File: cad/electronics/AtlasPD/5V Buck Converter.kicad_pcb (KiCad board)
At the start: 2 copper layers, 93.5 x 50.4 mm, 33 parts, among them J401 Conn_01x04, Q401 Q_Dual_NMOS_S1G1S2G2D2D2D1D1, U401 AP1509-50SG-13, U402 DS2777

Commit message: Refined PCB design, want to do final review later on before sending to Fab
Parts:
- added REF**: ESD-Logo_6.6x6mm_SilkScreen, Symbol:ESD-Logo_6.6x6mm_SilkScreen, F.Cu at (28.0, 73.4)
- added REF**: WEEE-Logo_4.2x6mm_SilkScreen, Symbol:WEEE-Logo_4.2x6mm_SilkScreen, F.Cu at (37.6, 73.3)
- added REF**: KiCad-Logo_5mm_Copper, Symbol:KiCad-Logo_5mm_Copper, B.Cu at (92.9, 79.1)
- R406: value RSNS -> 20m; footprint Resistor_SMD:R_0805_2012Metric -> Resistor_THT:R_Box_L13.0mm_W4.0mm_P9.00mm
- moved R406 2.49 mm to (71.8, 76.1), turned to 90 degrees
- moved U402 2.14 mm to (74.2, 80.3)
- moved REF** 1.88 mm to (19.8, 73.8)
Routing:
- net GND: track 2.34 -> 8.26 mm, vias 123 -> 121
- net Net-(C404-Pad1): track 17.1 -> 20.4 mm
- net /SRC: track 32.0 -> 34.6 mm
- net Net-(R407-Pad2): track 12.2 -> 14.5 mm
- net Net-(C403-Pad1): track 10.0 -> 7.95 mm
- net Net-(R401-Pad2): track 8.40 -> 10.0 mm
- net Net-(C405-Pad1): track 9.45 -> 10.8 mm
- net Net-(D402-Pad1): track 24.8 -> 25.9 mm
- net GNDPWR: track 10.1 -> 9.21 mm, vias 14 -> 13
- net Net-(D403-Pad2): track 10.8 -> 11.7 mm
- net Net-(R402-Pad2): track 10.7 -> 11.3 mm

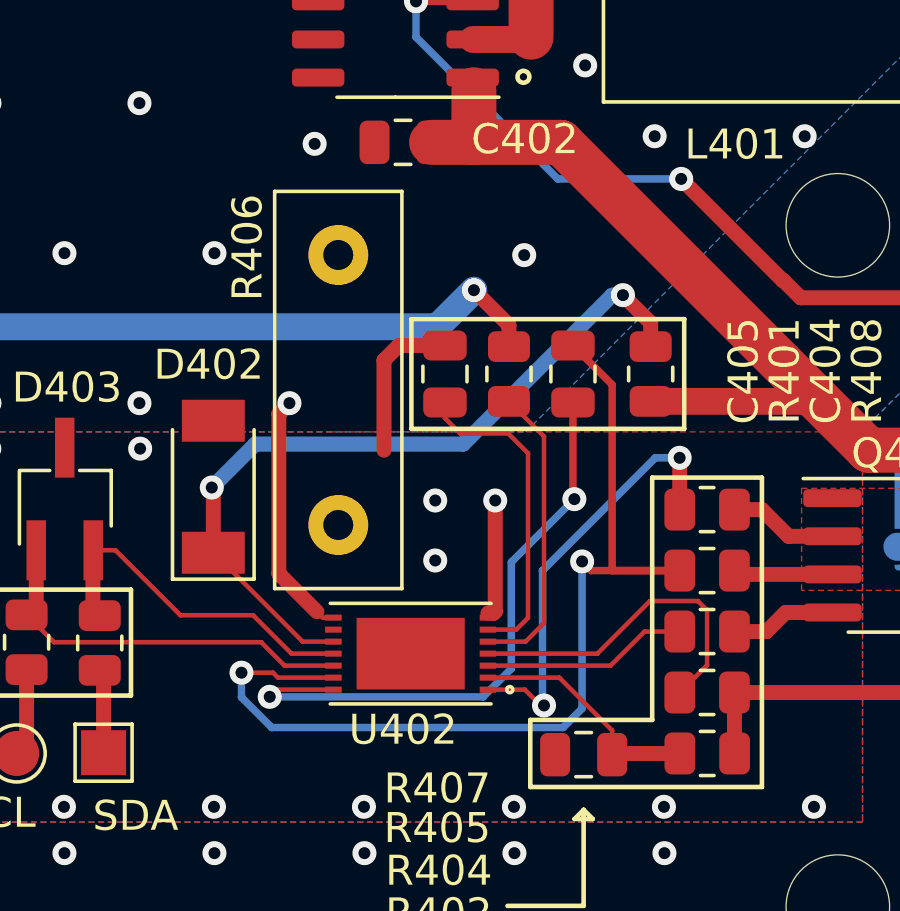
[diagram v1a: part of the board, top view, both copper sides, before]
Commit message: Simplified design layout
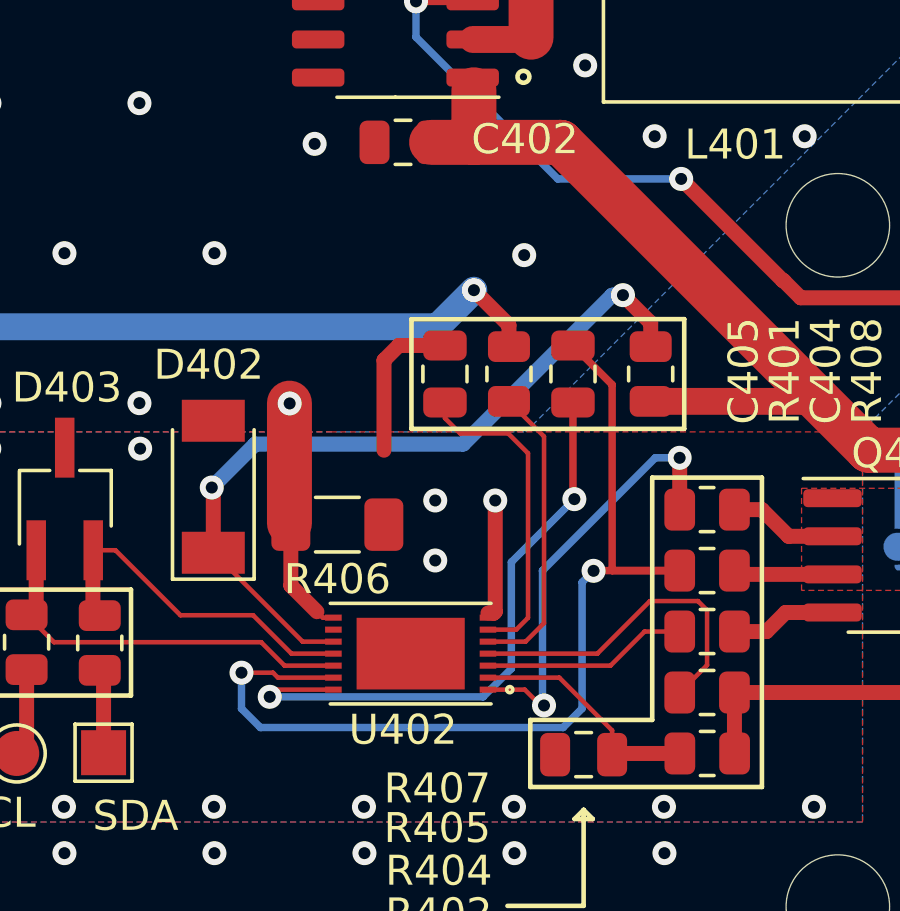
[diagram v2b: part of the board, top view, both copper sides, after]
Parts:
- R406: footprint Resistor_THT:R_Box_L13.0mm_W4.0mm_P9.00mm -> Resistor_SMD:R_1206_3216Metric_Pad1.30x1.75mm_HandSolder
- turned R406 to 180 degrees
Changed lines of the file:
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@@
       (net 23 "/SDA") (pinfunction "1") (pintype "passive"))
   )
+  (footprint "Resistor_SMD:R_1206_3216Metric_Pad1.30x1.75mm_HandSolder" (layer "F.Cu")
+    (at 71.75 76.04 180)
+    (descr "Resistor SMD 1206 (3216 Metric), square (rectangular) end terminal, IPC_7351 nominal with elongated pad for handsoldering. (Body size source: IPC-SM-782 page 72, https://www.pcb-3d.com/wordpress/wp-content/uploads/ipc-sm-782a_amendment_1_and_2.pdf), generated with kicad-footprint-generator")
+    (tags "resistor handsolder")
+    (property "Sheetfile" "5V Buck Converter.kicad_sch")
+    (property "Sheetname" "")
+    (attr smd)
+    (fp_text reference "R406" (at 0 -1.82) (layer "F.SilkS")
+      (effects (font (size 1 1) (thickness 0.15)))
+    )
+    (fp_text value "20m" (at 0 1.82) (layer "F.Fab")
+      (effects (font (size 1 1) (thickness 0.15)))
+    )
+    (fp_text user "${REFERENCE}" (at 0 0) (layer "F.Fab")
+      (effects (font (size 0.8 0.8) (thickness 0.12)))
+    )
+    (fp_line (start -0.727064 -0.91) (end 0.727064 -0.91) (layer "F.SilkS") (width 0.12))
+    (fp_line (start -0.727064 0.91) (end 0.727064 0.91) (layer "F.SilkS") (width 0.12))
+    (fp_line (start -2.45 -1.12) (end 2.45 -1.12) (layer "F.CrtYd") (width 0.05))
+    (fp_line (start -2.45 1.12) (end -2.45 -1.12) (layer "F.CrtYd") (width 0.05))
+    (fp_line (start 2.45 -1.12) (end 2.45 1.12) (layer "F.CrtYd") (width 0.05))
+    (fp_line (start 2.45 1.12) (end -2.45 1.12) (layer "F.CrtYd") (width 0.05))
+    (fp_line (start 1.6 -0.8) (end 1.6 0.8) (layer "F.Fab") (width 0.1))
+    (fp_line (start -1.6 -0.8) (end 1.6 -0.8) (layer "F.Fab") (width 0.1))
+    (fp_line (start 1.6 0.8) (end -1.6 0.8) (layer "F.Fab") (width 0.1))
+    (fp_line (start -1.6 0.8) (end -1.6 -0.8) (layer "F.Fab") (width 0.1))
+    (pad "1" smd roundrect locked (at -1.55 0 180) (size 1.3 1.75) (layers "F.Cu" "F.Paste" "F.Mask") (roundrect_rratio 0.192308)
+      (net 8 "GNDPWR") (pintype "passive"))
+    (pad "2" smd roundrect locked (at 1.55 0 180) (size 1.3 1.75) (layers "F.Cu" "F.Paste" "F.Mask") (roundrect_rratio 0.192308)
+      (net 1 "GND") (pintype "passive"))
+    (model "${KICAD6_3DMODEL_DIR}/Resistor_SMD.3dshapes/R_1206_3216Metric.wrl"
+      (offset (xyz 0 0 0))
+      (scale (xyz 1 1 1))
+      (rotate (xyz 0 0 0))
+    )
+  )
   (footprint "Package_TO_SOT_SMD:TSOT-23_HandSoldering" (layer "F.Cu")
     (at 62.6618 75.184 90)
@@
     )
   )
-  (footprint "Resistor_THT:R_Box_L13.0mm_W4.0mm_P9.00mm" (layer "F.Cu")
-    (at 71.7804 76.0518 90)
-    (descr "Resistor, Box series, Radial, pin pitch=9.00mm, 2W, length*width=13.0*4.0mm^2, http://www.produktinfo.conrad.com/datenblaetter/425000-449999/443860-da-01-de-METALLBAND_WIDERSTAND_0_1_OHM_5W_5Pr.pdf")
-    (tags "Resistor Box series Radial pin pitch 9.00mm 2W length 13.0mm width 4.0mm")
-    (property "Sheetfile" "5V Buck Converter.kicad_sch")
-    (property "Sheetname" "")
-    (attr through_hole)
-    (fp_text reference "R406" (at 9.2498 -3.0226 90) (layer "F.SilkS")
-      (effects (font (size 1 1) (thickness 0.15)))
-    )
-    (fp_text value "20m" (at 4.5 3.25 90) (layer "F.Fab")
-      (effects (font (size 1 1) (thickness 0.15)))
-    )
-    (fp_text user "${REFERENCE}" (at 4.5 0 90) (layer "F.Fab")
-      (effects (font (size 1 1) (thickness 0.15)))
-    )
-    (fp_line (start 11.12 -2.12) (end 11.12 2.12) (layer "F.SilkS") (width 0.12))
-    (fp_line (start -2.12 -2.12) (end 11.12 -2.12) (layer "F.SilkS") (width 0.12))
-    (fp_line (start -2.12 2.12) (end 11.12 2.12) (layer "F.SilkS") (width 0.12))
-    (fp_line (start -2.12 -2.12) (end -2.12 2.12) (layer "F.SilkS") (width 0.12))
-    (fp_line (start 11.25 -2.25) (end -2.25 -2.25) (layer "F.CrtYd") (width 0.05))
-    (fp_line (start -2.25 -2.25) (end -2.25 2.25) (layer "F.CrtYd") (width 0.05))
-    (fp_line (start -2.25 2.25) (end 11.25 2.25) (layer "F.CrtYd") (width 0.05))
-    (fp_line (start 11.25 2.25) (end 11.25 -2.25) (layer "F.CrtYd") (width 0.05))
-    (fp_line (start -2 2) (end 11 2) (layer "F.Fab") (width 0.1))
-    (fp_line (start 11 2) (end 11 -2) (layer "F.Fab") (width 0.1))
-    (fp_line (start -2 -2) (end -2 2) (layer "F.Fab") (width 0.1))
-    (fp_line (start 11 -2) (end -2 -2) (layer "F.Fab") (width 0.1))
-    (pad "1" thru_hole circle locked (at 0 0 90) (size 2 2) (drill 1) (layers *.Cu *.Mask)
-      (net 8 "GNDPWR") (pintype "passive"))
-    (pad "2" thru_hole circle locked (at 9 0 90) (size 2 2) (drill 1) (layers *.Cu *.Mask)
-      (net 1 "GND") (pintype "passive"))
-    (model "${KICAD6_3DMODEL_DIR}/Resistor_THT.3dshapes/R_Box_L13.0mm_W4.0mm_P9.00mm.wrl"
-      (offset (xyz 0 0 0))
-      (scale (xyz 1 1 1))
-      (rotate (xyz 0 0 0))
-    )
-  )
   (footprint "Resistor_SMD:R_0805_2012Metric" (layer "F.Cu")
     (at 84.079 83.6676 180)
@@
     (style (thickness 0.15) (arrow_length 1.27) (text_position_mode 0) (extension_height 0.58642) (extension_offset 0) keep_text_aligned)
   )
+  (segment (start 71.0692 78.9432) (end 70.2 78.074) (width 0.5) (layer "F.Cu") (net 1))
   (segment (start 71.2662 79.1402) (end 71.6177 79.1402) (width 0.1524) (layer "F.Cu") (net 1))
-  (segment (start 71.0692 78.9432) (end 69.7992 77.6732) (width 0.5) (layer "F.Cu") (net 1))
+  (segment (start 70.2 78.074) (end 70.2 76.04) (width 0.5) (layer "F.Cu") (net 1))
+  (segment (start 70.153 71.99) (end 70.153 75.993) (width 1.5) (layer "F.Cu") (net 1))
   (segment (start 71.0692 78.9432) (end 71.2662 79.1402) (width 0.1524) (layer "F.Cu") (net 1))
-  (segment (start 69.7992 77.6732) (end 69.7992 72.3438) (width 0.5) (layer "F.Cu") (net 1))
-  (segment (start 69.7992 72.3438) (end 70.153 71.99) (width 0.5) (layer "F.Cu") (net 1))
+  (segment (start 70.153 75.993) (end 70.2 76.04) (width 0.5) (layer "F.Cu") (net 1))
   (via (at 22.653 46.99) (size 0.8) (drill 0.4) (layers "F.Cu" "B.Cu") (net 1))
   (via (at 27.653 46.99) (size 0.8) (drill 0.4) (layers "F.Cu" "B.Cu") (net 1))
@@
   (via (at 67.653 66.99) (size 0.8) (drill 0.4) (layers "F.Cu" "B.Cu") (net 1))
   (via (at 77.978 67.056) (size 0.8) (drill 0.4) (layers "F.Cu" "B.Cu") (net 1))
-  (via (at 70.153 71.99) (size 0.8) (drill 0.4) (layers "F.Cu" "B.Cu") (net 1))
+  (via (at 70.16 72) (size 0.8) (drill 0.4) (layers "F.Cu" "B.Cu") (net 1))
   (via (at 65.153 71.99) (size 0.8) (drill 0.4) (layers "F.Cu" "B.Cu") (net 1))
   (via (at 80.01 60.7314) (size 0.8) (drill 0.4) (layers "F.Cu" "B.Cu") (net 1))
@@
   (segment (start 77.55 80.84) (end 76.610556 81.779444) (width 0.25) (layer "B.Cu") (net 10))
   (segment (start 77.55 77.29) (end 77.55 80.84) (width 0.25) (layer "B.Cu") (net 10))
-  (segment (start 80.2132 77.5716) (end 83.1615 77.5716) (width 0.25) (layer "F.Cu") (net 11))
+  (segment (start 80.29 77.58) (end 80.2984 77.5716) (width 0.25) (layer "F.Cu") (net 11))
   (segment (start 80.909089 77.5716) (end 83.1615 77.5716) (width 0.25) (layer "F.Cu") (net 11))
   (segment (start 71.6177 81.140201) (end 69.770201 81.140201) (width 0.1524) (layer "F.Cu") (net 11))
+  (segment (start 80.2984 77.5716) (end 83.1615 77.5716) (width 0.25) (layer "F.Cu") (net 11))
   (segment (start 69.6052 80.9752) (end 68.5546 80.9752) (width 0.1524) (layer "F.Cu") (net 11))
   (segment (start 80.909089 71.373889) (end 80.909089 77.5716) (width 0.25) (layer "F.Cu") (net 11))
   (segment (start 69.770201 81.140201) (end 69.6052 80.9752) (width 0.1524) (layer "F.Cu") (net 11))
   (segment (start 79.6036 70.0684) (end 80.909089 71.373889) (width 0.25) (layer "F.Cu") (net 11))
-  (segment (start 79.9084 77.2668) (end 80.2132 77.5716) (width 0.25) (layer "F.Cu") (net 11))
-  (via (at 79.9084 77.2668) (size 0.8) (drill 0.4) (layers "F.Cu" "B.Cu") (net 11))
+  (via (at 80.29 77.58) (size 0.8) (drill 0.4) (layers "F.Cu" "B.Cu") (net 11))
   (via (at 68.5546 80.9752) (size 0.8) (drill 0.4) (layers "F.Cu" "B.Cu") (net 11))
-  (segment (start 79.9084 82.169) (end 79.9084 77.2668) (width 0.25) (layer "B.Cu") (net 11))
-  (segment (start 69.564249 82.804) (end 79.2734 82.804) (width 0.25) (layer "B.Cu") (net 11))
-  (segment (start 68.5546 81.794351) (end 69.564249 82.804) (width 0.25) (layer "B.Cu") (net 11))
-  (segment (start 79.2734 82.804) (end 79.9084 82.169) (width 0.25) (layer "B.Cu") (net 11))
-  (segment (start 68.5546 80.9752) (end 68.5546 81.794351) (width 0.25) (layer "B.Cu") (net 11))
+  (segment (start 80.29 77.58) (end 79.9084 77.9616) (width 0.25) (layer "B.Cu") (net 11))
+  (segment (start 79.2734 82.804) (end 69.184 82.804) (width 0.25) (layer "B.Cu") (net 11))
+  (segment (start 79.9084 82.169) (end 79.2734 82.804) (width 0.25) (layer "B.Cu") (net 11))
+  (segment (start 69.184 82.804) (end 68.5546 82.1746) (width 0.25) (layer "B.Cu") (net 11))
+  (segment (start 68.5546 82.1746) (end 68.5546 80.9752) (width 0.25) (layer "B.Cu") (net 11))
+  (segment (start 79.9084 77.9616) (end 79.9084 82.169) (width 0.25) (layer "B.Cu") (net 11))
   (segment (start 75.3364 72.4916) (end 75.8444 72.9996) (width 0.1524) (layer "F.Cu") (net 12))
   (segment (start 77.4446 72.9996) (end 78.105 73.66) (width 0.1524) (layer "F.Cu") (net 12))
